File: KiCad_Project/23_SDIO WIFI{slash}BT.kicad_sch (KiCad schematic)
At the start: 19 parts, among them U15 2.4GHz, X3 26MHz

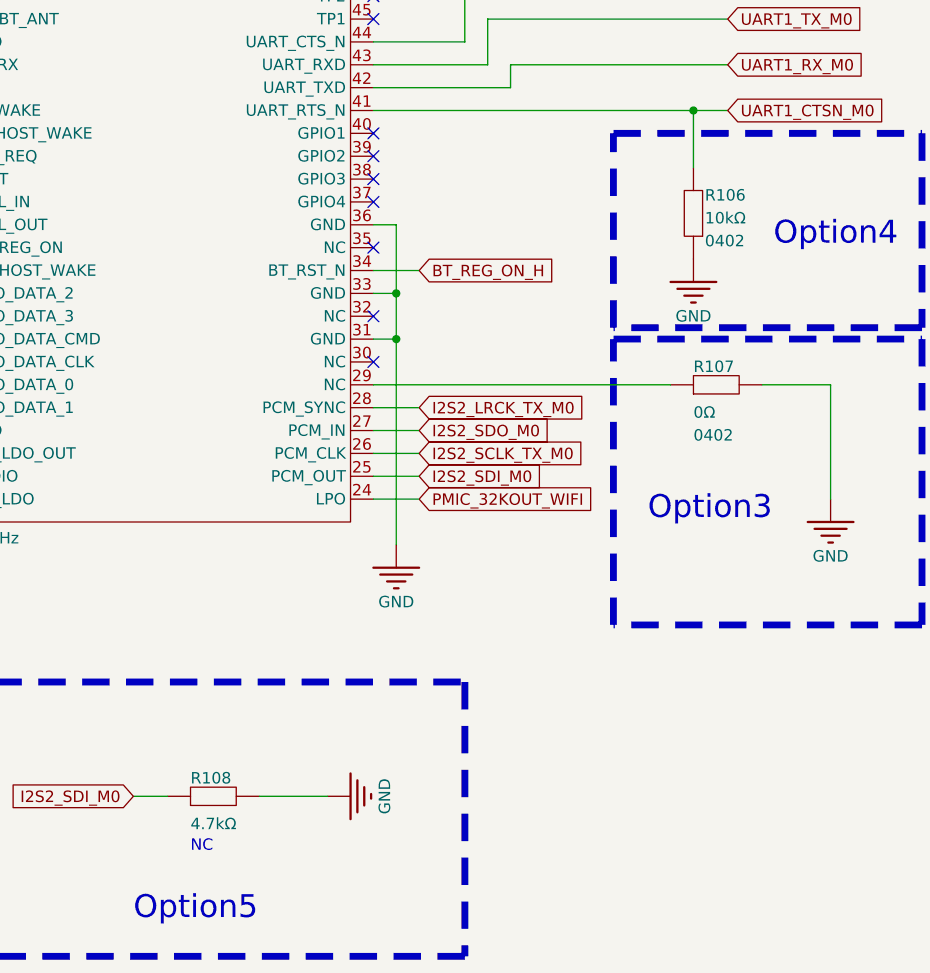
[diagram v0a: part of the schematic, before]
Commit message: Update additional PCBs
Add WIFI PCB to get best antenna
Add Display Debbugger to get interface pinout
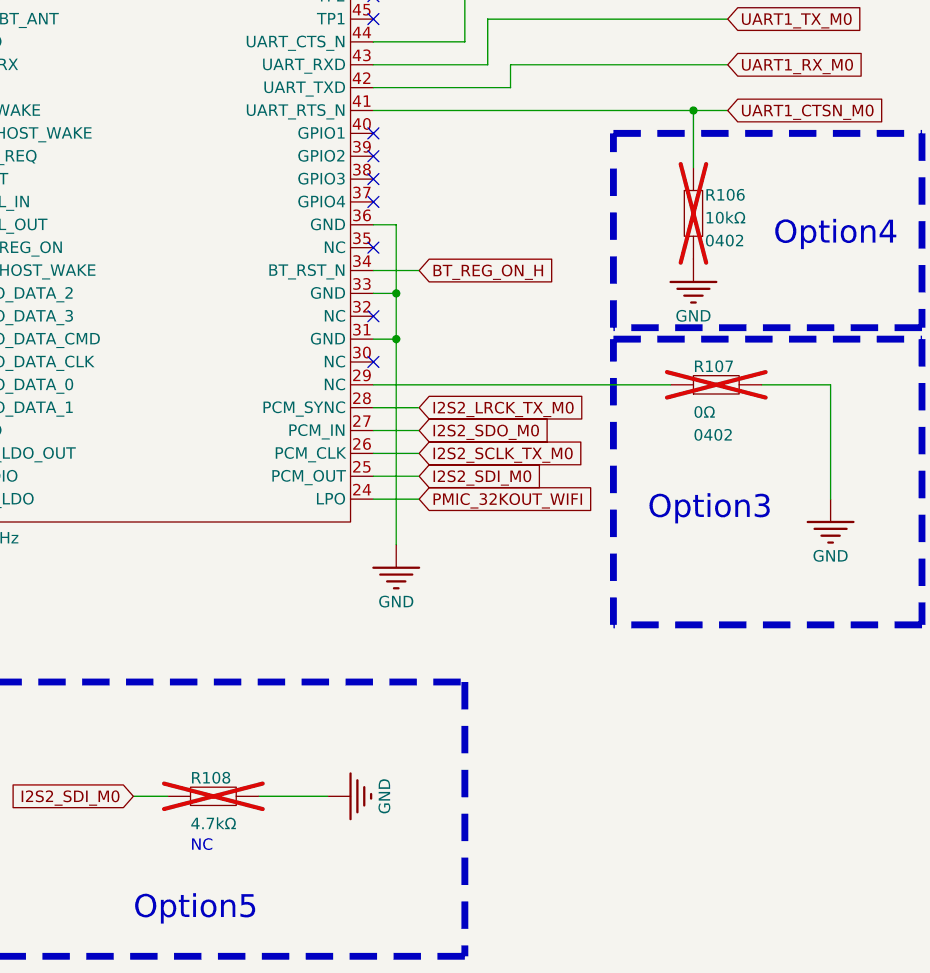
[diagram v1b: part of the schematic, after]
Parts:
- R106, R107, R108: now not fitted; now left out of the parts list
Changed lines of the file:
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@@
 		(unit 1)
 		(exclude_from_sim no)
-		(in_bom yes)
+		(in_bom no)
 		(on_board yes)
-		(dnp no)
+		(dnp yes)
 		(property "Reference" "R107"
 			(at 306.07 92.71 0)
@@
 		(unit 1)
 		(exclude_from_sim no)
-		(in_bom yes)
+		(in_bom no)
 		(on_board yes)
-		(dnp no)
+		(dnp yes)
 		(property "Reference" "R108"
 			(at 250.19 138.43 0)
@@
 		(unit 1)
 		(exclude_from_sim no)
-		(in_bom yes)
+		(in_bom no)
 		(on_board yes)
-		(dnp no)
+		(dnp yes)
 		(property "Reference" "R106"
 			(at 307.34 73.66 90)
